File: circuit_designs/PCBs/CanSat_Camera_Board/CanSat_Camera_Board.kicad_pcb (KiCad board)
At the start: 2 copper layers, 55 x 80 mm, 10 parts

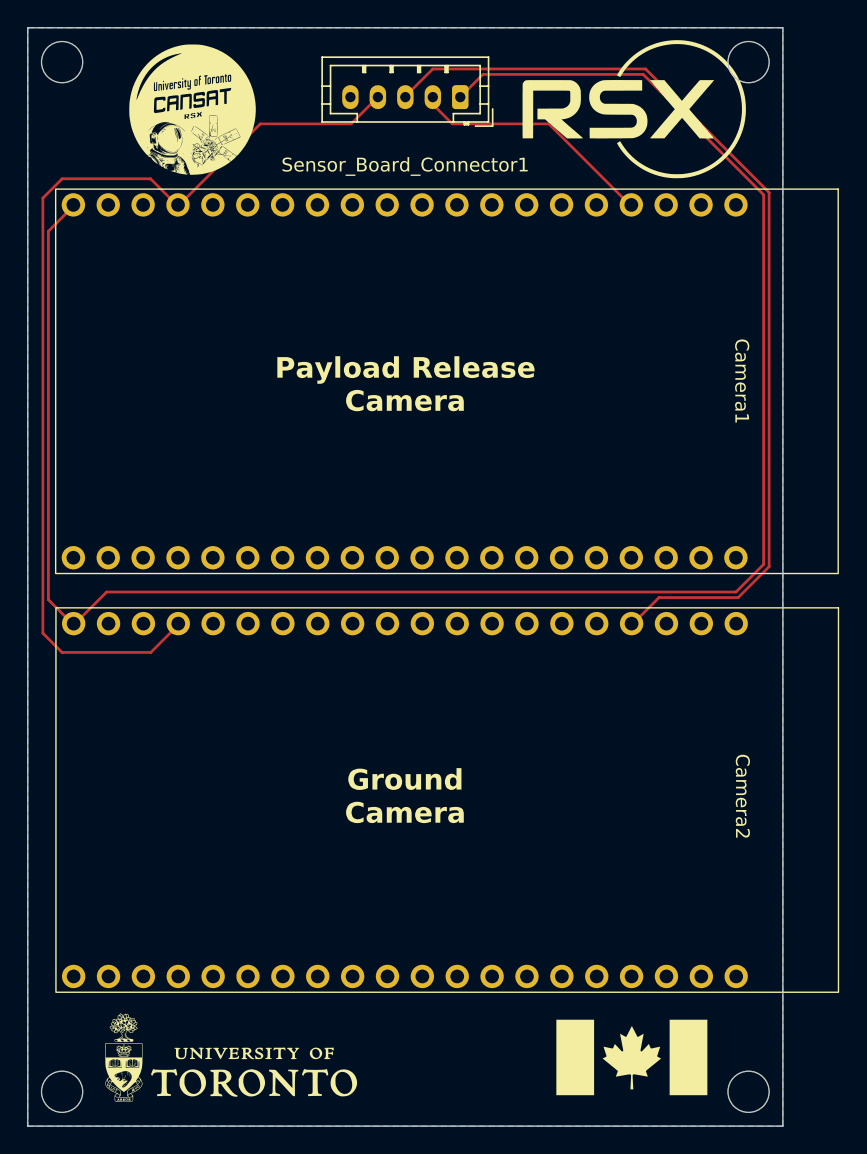
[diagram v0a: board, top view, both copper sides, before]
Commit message: Updating camera and sensor PCBs
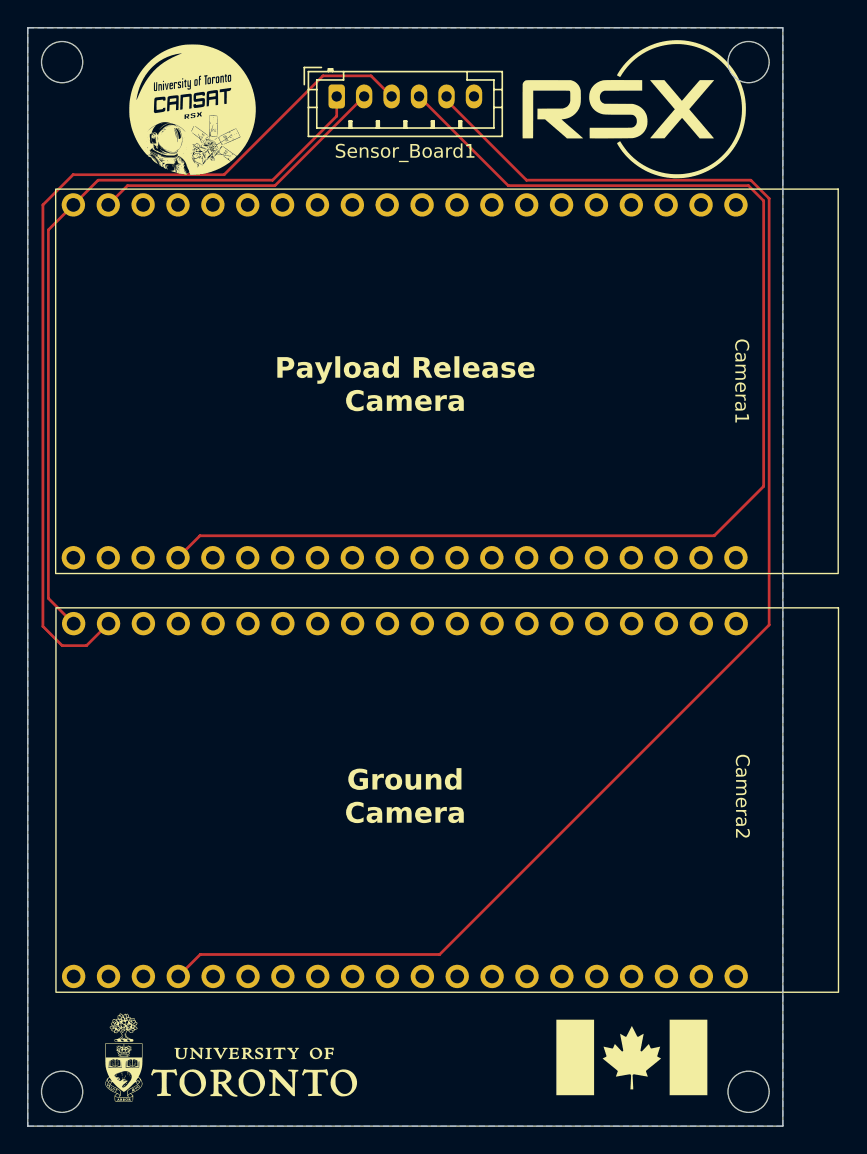
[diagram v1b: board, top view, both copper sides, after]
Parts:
- removed Sensor_Board_Connector1: Conn_01x05_Pin, Connector_JST:JST_PH_B5B-PH-K_1x05_P2.00mm_Vertical
- added Sensor_Board1: Conn_01x06_Pin, Connector_JST:JST_PH_B6B-PH-K_1x06_P2.00mm_Vertical, F.Cu at (145.0, 65.0)
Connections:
- Camera1 pad J2-17: SIG1 -> unconnected-(Camera1-GPIO12-PadJ2-17)
- Camera1 pad J2-19: unconnected-(Camera1-GPIO14-PadJ2-19) -> SIGNAL1
- Camera1 pad J2-4: CAM1 -> unconnected-(Camera1-GPIO5-PadJ2-4)
- Camera1 pad J3-17: unconnected-(Camera1-GPIO21-PadJ3-17) -> DATA1
- Camera2 pad J2-17: SIG1 -> unconnected-(Camera2-GPIO12-PadJ2-17)
- Camera2 pad J2-19: unconnected-(Camera2-GPIO14-PadJ2-19) -> SIGNAL2
- Camera2 pad J2-4: CAM2 -> unconnected-(Camera2-GPIO5-PadJ2-4)
- Camera2 pad J3-17: unconnected-(Camera2-GPIO21-PadJ3-17) -> DATA2
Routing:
- net DATA2: track 0.00 -> 111.5 mm
- net DATA1: track 0.00 -> 93.9 mm
- net VCC: track 138.0 -> 55.9 mm
- net SIG1: track 72.1 -> 0.00 mm
- net CAM2: track 70.1 -> 0.00 mm
- net SIGNAL2: track 0.00 -> 66.6 mm
- net SIGNAL1: track 0.00 -> 21.9 mm
- net CAM1: track 18.6 -> 0.00 mm

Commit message: Final review submission of all CanSat PCB boards and corresponding custom KiCad 3D models, footprints, and symbols
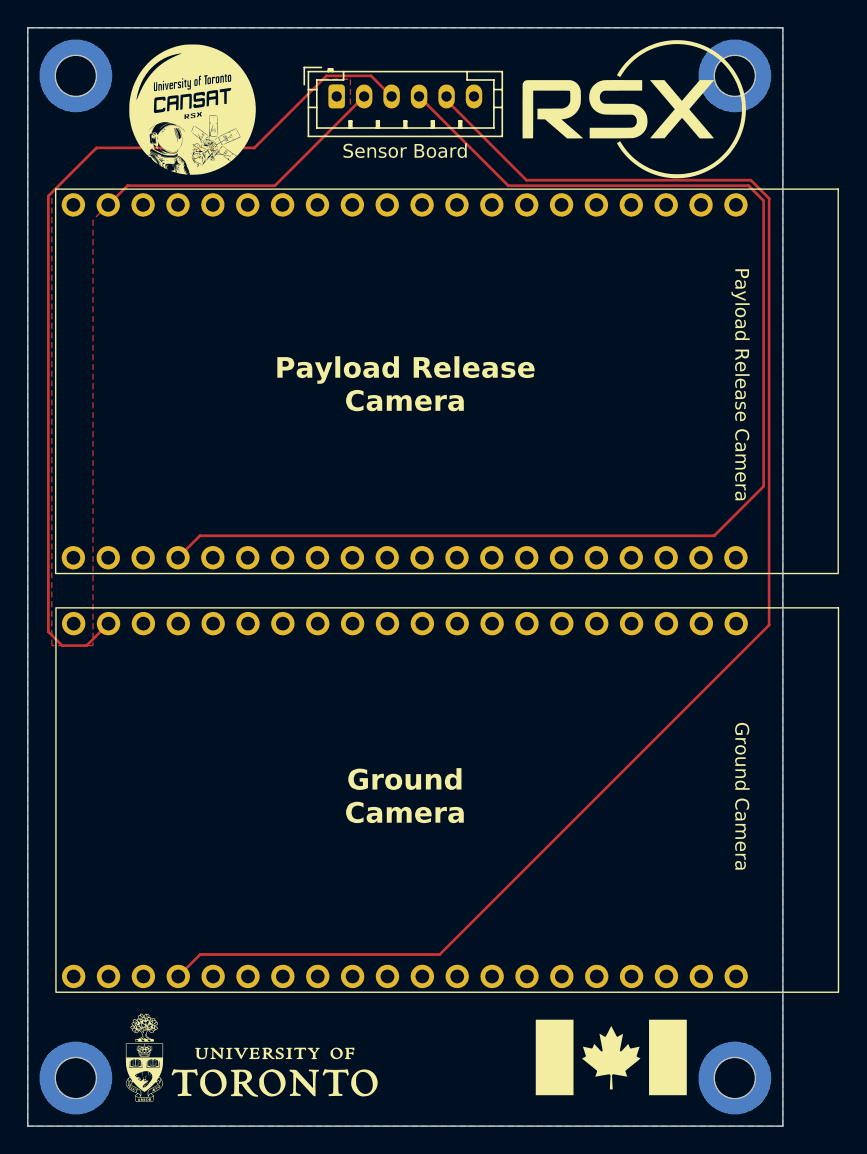
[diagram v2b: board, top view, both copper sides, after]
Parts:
- removed the G*** at (150.0, 85.0)
- added G***: LOGO, Graphics:cansat_logo_2, B.Cu at (150.0, 85.5)
- added REF**: WA-SMSI_9774030243, DigiKey:WA-SMSI_9774030243, B.Cu at (126.0, 63.5)
- added REF**: WA-SMSI_9774030243, DigiKey:WA-SMSI_9774030243, B.Cu at (126.0, 136.5)
- added REF**: WA-SMSI_9774030243, DigiKey:WA-SMSI_9774030243, B.Cu at (174.0, 63.5)
- added REF**: WA-SMSI_9774030243, DigiKey:WA-SMSI_9774030243, B.Cu at (174.0, 136.5)
- Freenove_ESP32-S3-WROOM_CAM_Board_U1: renamed from Camera1; value Freenove_ESP32-S3-WROOM_CAM_Board -> Payload Release Camera
- Freenove_ESP32-S3-WROOM_CAM_Board_U2: renamed from Camera2; value Freenove_ESP32-S3-WROOM_CAM_Board -> Ground Camera
- J1: renamed from Sensor_Board1; value Conn_01x06_Pin -> Sensor Board
- moved G*** 1.50 mm to (165.0, 135.0)
- moved G*** 1.50 mm to (131.0, 135.0)
- moved G*** 1.50 mm to (140.5, 136.0)
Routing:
- net VCC: track 55.9 -> 0.59 mm
- added copper zone on F.Cu, net VCC
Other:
- outline, holes or cut-outs redrawn
- board text added: "DATA1"
- board text added: "DATA2"
- board text added: "SIG1"
- board text added: "SIG2"
- board text removed: "CAM1"
- board text removed: "CAM2"
- board text removed: "SIG"

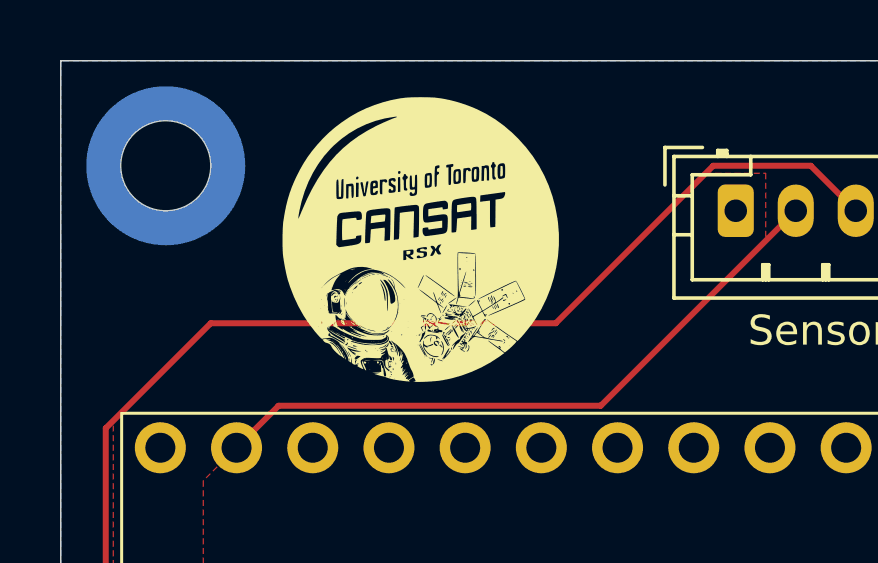
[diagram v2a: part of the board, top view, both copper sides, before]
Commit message: fixed errors and exposed copper for thermal pads
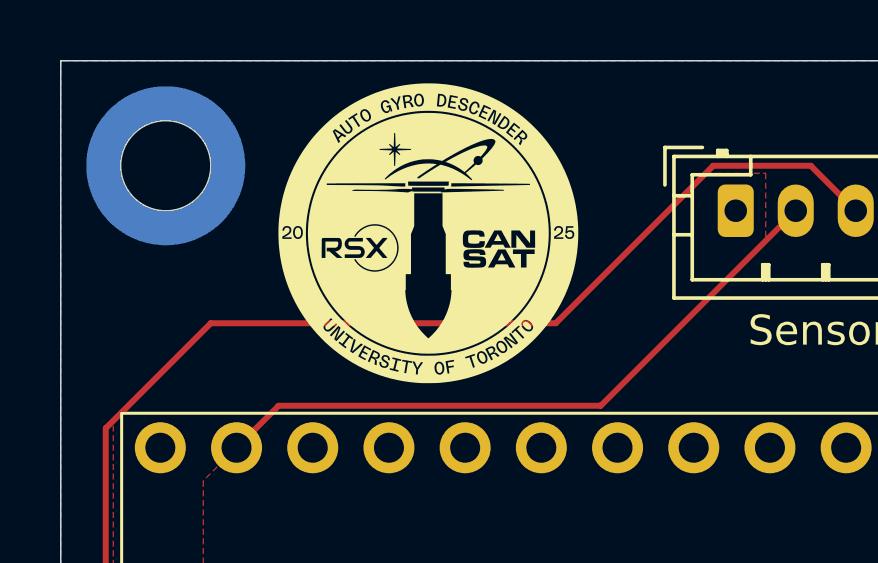
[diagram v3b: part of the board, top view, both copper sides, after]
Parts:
- removed the G*** at (134.5, 66.0)
- added G***: LOGO, Graphics:logo, F.Cu at (134.8, 65.8)
